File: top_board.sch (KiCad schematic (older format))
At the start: 33 parts, among them IC1 MCP6001T-I_OT, J3 UFL-Conn, J4 SWD, J5 Console, Q1 CMBT2222A, Q2 PT204-6C, SW1 SW_Push, U1 EESAMR34J18-V1_CT

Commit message: Agregado modulo HLW8032
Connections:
- net Relay: now also U1.19 (PA15); no longer U1.21 (PA14)
- net Enery_Tx: now reaches U1.23 (PA17)
- new net Enery_Pulses: U1.21 (PA14)
- no-connect marks 17 -> 15
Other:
- moved on the sheet: BAT1
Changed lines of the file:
@@
 L power:GNDD #PWR?
 U 1 1 5F8D480F
-P 3050 6100
+P 3150 6150
 AR Path="/5F8D480F" Ref="#PWR?"  Part="1"
 AR Path="/5F84ED08/5F8D480F" Ref="#PWR020"  Part="1"
-F 0 "#PWR020" H 3050 5850 50  0001 C CNN
-F 1 "GNDD" H 3054 5945 50  0000 C CNN
-F 2 "" H 3050 6100 50  0001 C CNN
-F 3 "" H 3050 6100 50  0001 C CNN
-	1    3050 6100
-	1    0    0    -1
-$EndComp
-Wire Wire Line
-	3050 6050 3050 6100
-Wire Wire Line
-	2850 6050 2850 6100
-Wire Wire Line
-	2850 6100 3050 6100
-Connection ~ 3050 6100
+F 0 "#PWR020" H 3150 5900 50  0001 C CNN
+F 1 "GNDD" H 3154 5995 50  0000 C CNN
+F 2 "" H 3150 6150 50  0001 C CNN
+F 3 "" H 3150 6150 50  0001 C CNN
+	1    3150 6150
+	1    0    0    -1
+$EndComp
 $Comp
 L power:GNDD #PWR?
@@
 Text Label 3750 5250 0    50   ~ 0
 Led2
-Text Label 3750 5650 0    50   ~ 0
+Text Label 2950 6300 2    50   ~ 0
 Relay
 Text Label 2250 6550 2    50   ~ 0
@@
 NoConn ~ 3550 4950
 NoConn ~ 3550 5050
-NoConn ~ 3550 5450
 NoConn ~ 3550 5550
 NoConn ~ 2750 6050
-NoConn ~ 2950 6050
 NoConn ~ 2450 6050
 NoConn ~ 2150 6050
@@
 L Connector_Generic:Conn_01x02 BAT?
 U 1 1 5F8EE8E1
-P 9650 5800
+P 7850 5750
 AR Path="/5F8EE8E1" Ref="BAT?"  Part="1"
 AR Path="/5F84ED08/5F8EE8E1" Ref="BAT1"  Part="1"
-F 0 "BAT1" H 9568 6017 50  0000 C CNN
-F 1 "Conn_01x02" H 9568 5926 50  0000 C CNN
-F 2 "Connector_PinHeader_2.54mm:PinHeader_1x02_P2.54mm_Vertical" H 9650 5800 50  0001 C CNN
-F 3 "~" H 9650 5800 50  0001 C CNN
-	1    9650 5800
+F 0 "BAT1" H 7768 5967 50  0000 C CNN
+F 1 "Conn_01x02" H 7768 5876 50  0000 C CNN
+F 2 "Connector_PinHeader_2.54mm:PinHeader_1x02_P2.54mm_Vertical" H 7850 5750 50  0001 C CNN
+F 3 "~" H 7850 5750 50  0001 C CNN
+	1    7850 5750
 	-1   0    0    -1
 $EndComp
@@
 L power:GNDD #PWR?
 U 1 1 5F8EE8E7
-P 9950 5950
+P 8150 5900
 AR Path="/5F8EE8E7" Ref="#PWR?"  Part="1"
 AR Path="/5F84ED08/5F8EE8E7" Ref="#PWR018"  Part="1"
-F 0 "#PWR018" H 9950 5700 50  0001 C CNN
-F 1 "GNDD" H 9954 5795 50  0000 C CNN
-F 2 "" H 9950 5950 50  0001 C CNN
-F 3 "" H 9950 5950 50  0001 C CNN
-	1    9950 5950
-	1    0    0    -1
-$EndComp
-Text Label 9950 5800 0    50   ~ 0
+F 0 "#PWR018" H 8150 5650 50  0001 C CNN
+F 1 "GNDD" H 8154 5745 50  0000 C CNN
+F 2 "" H 8150 5900 50  0001 C CNN
+F 3 "" H 8150 5900 50  0001 C CNN
+	1    8150 5900
+	1    0    0    -1
+$EndComp
+Text Label 8150 5750 0    50   ~ 0
 +3.3v
 Wire Wire Line
-	9850 5800 9950 5800
-Wire Wire Line
-	9850 5900 9950 5900
-Wire Wire Line
-	9950 5900 9950 5950
-Text HLabel 6950 5700 2    50   Input ~ 0
+	8050 5750 8150 5750
+Wire Wire Line
+	8050 5850 8150 5850
+Wire Wire Line
+	8150 5850 8150 5900
+Text HLabel 10500 1200 2    50   Input ~ 0
 3.3v
-Text HLabel 6950 6300 2    50   UnSpc ~ 0
+Text HLabel 10500 1050 2    50   UnSpc ~ 0
 GND
-Text HLabel 6950 5850 2    50   Output ~ 0
+Text HLabel 10500 900  2    50   Output ~ 0
 OpenC
-Text HLabel 6950 6000 2    50   Input ~ 0
+Text HLabel 10500 1350 2    50   Input ~ 0
 PIR
-Text HLabel 6950 6150 2    50   Output ~ 0
+Text HLabel 10500 1500 2    50   Output ~ 0
 Relay
-Text Label 6800 5700 2    50   ~ 0
+Text Label 10350 1200 2    50   ~ 0
 +3.3v
 $Comp
 L power:GNDD #PWR?
 U 1 1 5F8F5116
-P 6550 6300
+P 10000 1050
 AR Path="/5F8F5116" Ref="#PWR?"  Part="1"
 AR Path="/5F84ED08/5F8F5116" Ref="#PWR021"  Part="1"
-F 0 "#PWR021" H 6550 6050 50  0001 C CNN
-F 1 "GNDD" H 6554 6145 50  0000 C CNN
-F 2 "" H 6550 6300 50  0001 C CNN
-F 3 "" H 6550 6300 50  0001 C CNN
-	1    6550 6300
-	1    0    0    -1
-$EndComp
-Wire Wire Line
-	6550 6300 6950 6300
-Wire Wire Line
-	6800 5700 6950 5700
-Text Label 6800 5850 2    50   ~ 0
+F 0 "#PWR021" H 10000 800 50  0001 C CNN
+F 1 "GNDD" H 10004 895 50  0000 C CNN
+F 2 "" H 10000 1050 50  0001 C CNN
+F 3 "" H 10000 1050 50  0001 C CNN
+	1    10000 1050
+	1    0    0    -1
+$EndComp
+Wire Wire Line
+	10350 1200 10500 1200
+Text Label 10350 900  2    50   ~ 0
 OpenC
-Text Label 6800 6000 2    50   ~ 0
+Text Label 10350 1350 2    50   ~ 0
 PIR
-Text Label 6800 6150 2    50   ~ 0
+Text Label 10350 1500 2    50   ~ 0
 Relay
 Wire Wire Line
-	6800 5850 6950 5850
-Wire Wire Line
-	6800 6000 6950 6000
-Wire Wire Line
-	6800 6150 6950 6150
+	10350 900  10500 900
+Wire Wire Line
+	10350 1350 10500 1350
+Wire Wire Line
+	10350 1500 10500 1500
 $Comp
 L power:PWR_FLAG #FLG?
@@
 	1    0    0    -1
 $EndComp
+Text Label 10300 1800 2    50   ~ 0
+Energy_Pulses
+Text Label 10300 1650 2    50   ~ 0
+Enery_Tx
+Text HLabel 10500 1650 2    50   Input ~ 0
+Enery_Tx
+Text HLabel 10500 1800 2    50   Input ~ 0
+Enery_Pulses
+Wire Wire Line
+	10300 1650 10500 1650
+Wire Wire Line
+	10300 1800 10500 1800
+Wire Wire Line
+	10000 1050 10500 1050
+Text Label 3750 5650 0    50   ~ 0
+Energy_Pulses
+Text Label 3750 5450 0    50   ~ 0
+Enery_Tx
+Wire Wire Line
+	3550 5450 3750 5450
+Wire Wire Line
+	2950 6050 2950 6300
+Wire Wire Line
+	3150 6150 3050 6150
+Wire Wire Line
+	2850 6150 2850 6050
+Wire Wire Line
+	3050 6050 3050 6150
+Connection ~ 3050 6150
+Wire Wire Line
+	3050 6150 2850 6150
 $EndSCHEMATC

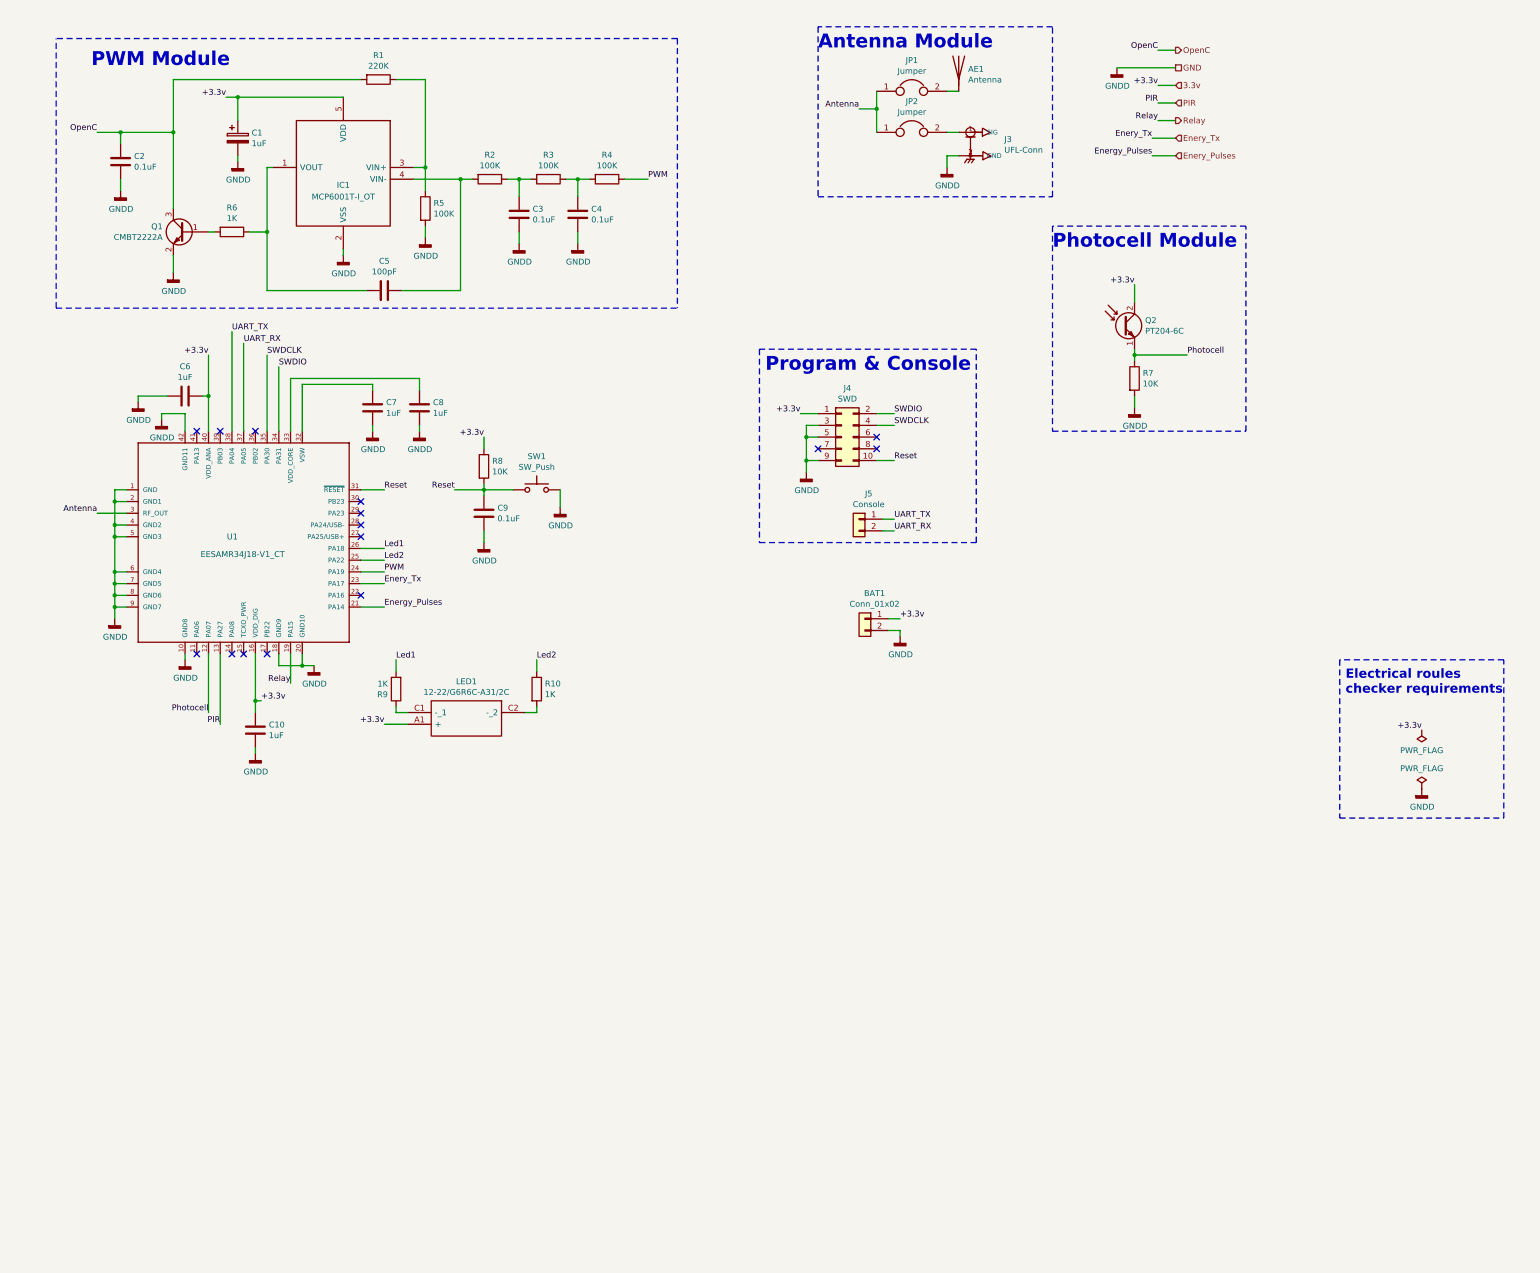
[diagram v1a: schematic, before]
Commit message: Esquematico reordenado
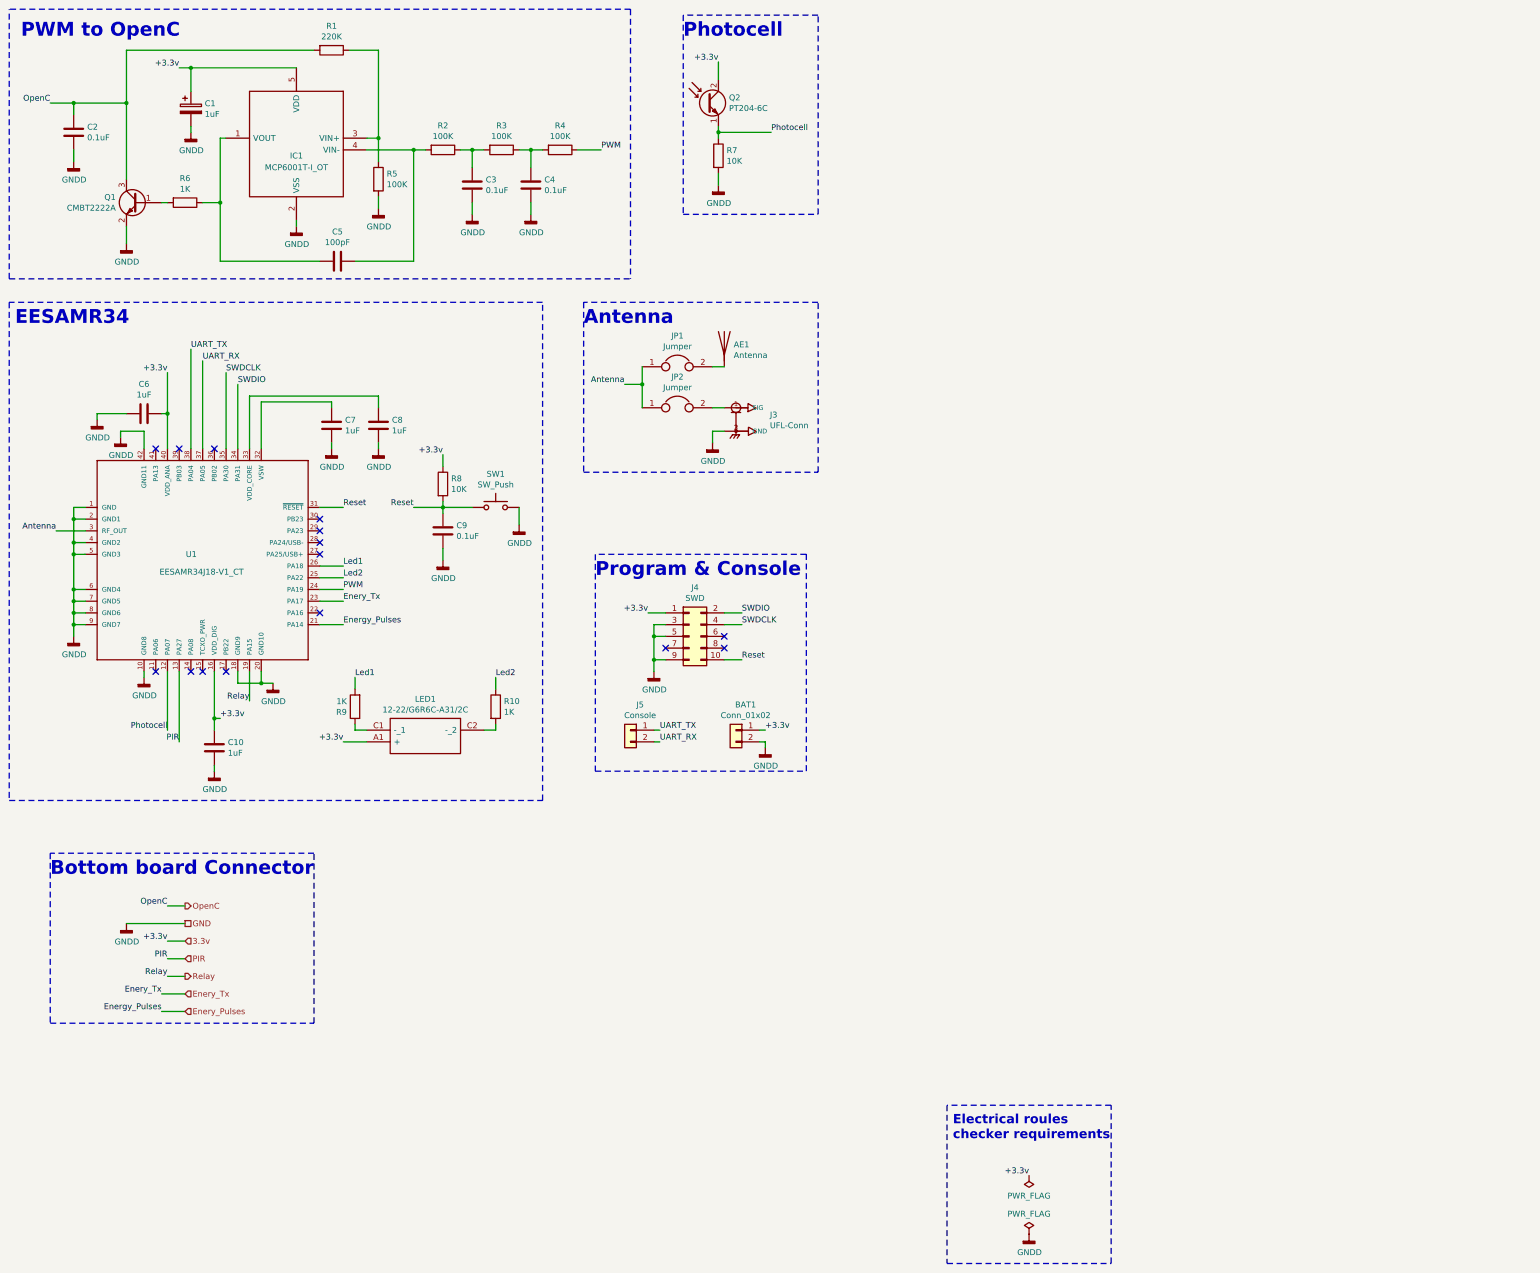
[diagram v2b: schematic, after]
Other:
- note added: "Antenna"
- note added: "Bottom board Connector"
- note added: "EESAMR34"
- note added: "PWM to OpenC"
- note added: "Photocell"
- note removed: "Antenna Module"
- note removed: "PWM Module"
- note removed: "Photocell Module"
- moved on the sheet: AE1, BAT1, C1, C10, C2, C3, C4, C5, C6, C7, C8, C9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
